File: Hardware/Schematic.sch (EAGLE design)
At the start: 89 parts, among them IC1 XC6220A331MR-G, IC2 BD5229G-TR, J1 SAMACSYS_PARTS_USB4110-GF-A, J2 FH34SRJ-24S-0.5SH_99_, J4 112A-TAAR-R03_ATTEND, Q1 20V/4.2A/52mΩ/1.4W, Q2 SI1308EDL-T1-GE3, Q3 20V/4.2A/52mΩ/1.4W, U1 ESP32_WROVER_SPARKFUN-IC-POWE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, U2 ESP32-C6-WROOM-1-N8, U3 ESP32_WROVER_BME680_BME680, U4 MAX17048G+T10, U5 DS3231SN#

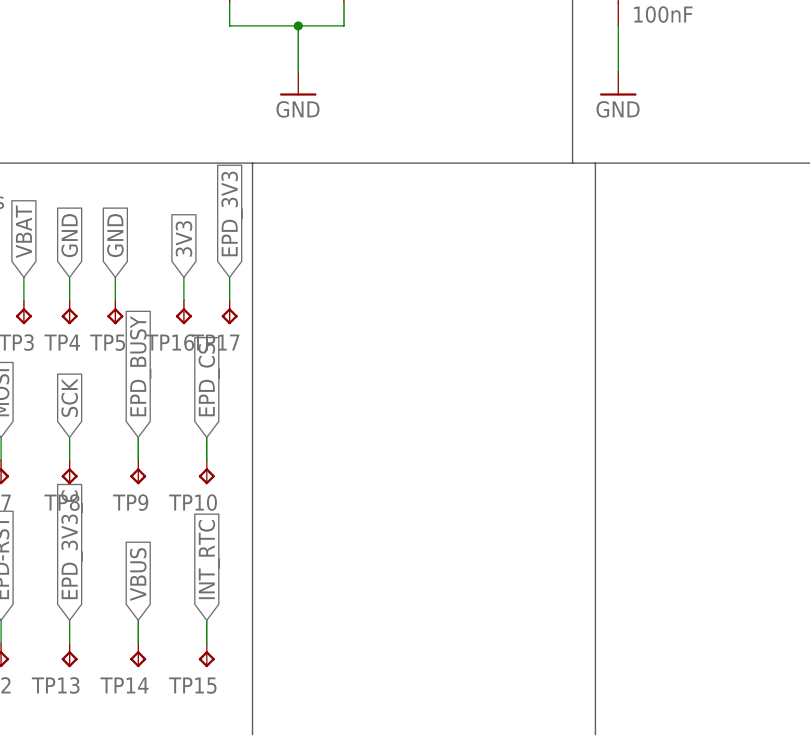
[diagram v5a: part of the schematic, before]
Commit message: add Qwiic /Stemma QT
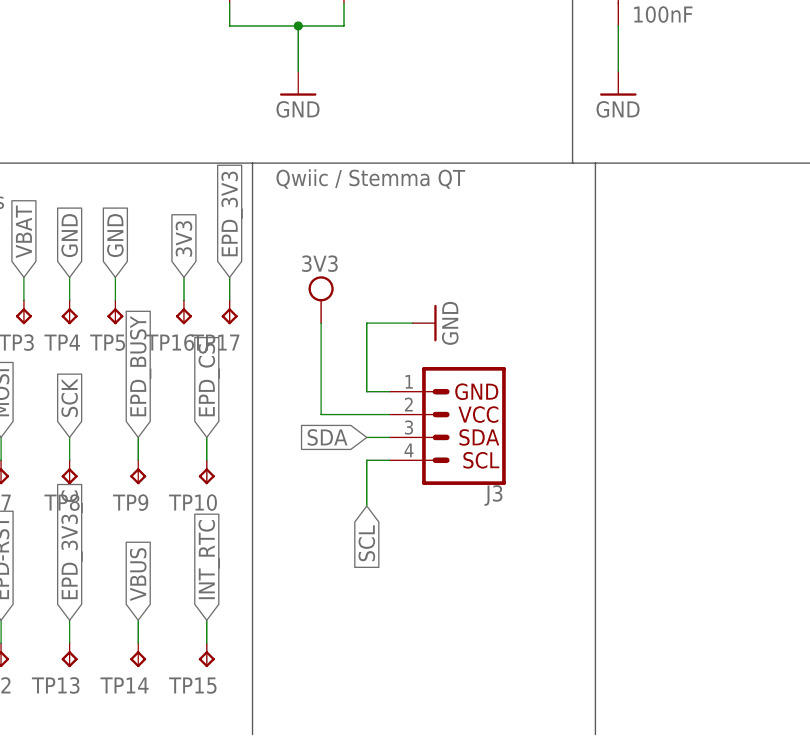
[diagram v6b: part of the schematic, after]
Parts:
- added J3: QWIIC_RIGHT_ANGLE, DeskAssistant v19 v1.flbr:QWIIC_CONNECTORJS-1MM
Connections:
- net 3V3: now also J3.2
- net GND: now also J3.1
- net SCL: now also J3.4
- net SDA: now also J3.3
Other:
- note added: "Qwiic / Stemma QT"
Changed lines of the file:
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@@
 <part name="TP16" library="DeskAssistant v19 v1.flbr" library_urn="urn:adsk.wipprod:fs.file:vf.vVvdDOfaSfavM5thX5SjWw" deviceset="TP" device="TP20R"/>
 <part name="TP17" library="DeskAssistant v19 v1.flbr" library_urn="urn:adsk.wipprod:fs.file:vf.vVvdDOfaSfavM5thX5SjWw" deviceset="TP" device="TP20R"/>
+<part name="J3" library="DeskAssistant v19 v1.flbr" library_urn="urn:adsk.wipprod:fs.file:vf.vVvdDOfaSfavM5thX5SjWw" deviceset="QWIIC_CONNECTOR" device="JS-1MM" package3d_urn="urn:adsk.eagle:package:41390393/1" value="QWIIC_RIGHT_ANGLE"/>
+<part name="SUPPLY14" library="DeskAssistant v19 v1.flbr" library_urn="urn:adsk.wipprod:fs.file:vf.vVvdDOfaSfavM5thX5SjWw" deviceset="3V3-CIRCLE" device="" value="3V3"/>
+<part name="GND41" library="DeskAssistant v19 v1.flbr" library_urn="urn:adsk.wipprod:fs.file:vf.vVvdDOfaSfavM5thX5SjWw" deviceset="GND" device=""/>
 </parts>
 <sheets>
@@
 <text x="-160.02" y="81.28" size="1.778" layer="95"> RTC Module DS3231SN</text>
 <text x="-10.16" y="81.28" size="1.778" layer="95">Test Pads</text>
+<text x="30.48" y="83.82" size="1.778" layer="95">Qwiic / Stemma QT</text>
 </plain>
 <instances>
@@
 <attribute name="NAME" x="26.67" y="67.31" size="1.778" layer="95" rot="R180"/>
 <attribute name="TP_SIGNAL_NAME" x="24.13" y="69.85" size="1.778" layer="97" rot="R180"/>
+</instance>
+<instance part="J3" gate="J1" x="50.8" y="58.42" smashed="yes" rot="R180">
+<attribute name="NAME" x="55.88" y="50.546" size="1.778" layer="95" font="vector" rot="R180"/>
+</instance>
+<instance part="SUPPLY14" gate="G$1" x="35.56" y="71.12" smashed="yes">
+<attribute name="VALUE" x="35.433" y="74.295" size="1.778" layer="96" align="bottom-center"/>
+</instance>
+<instance part="GND41" gate="1" x="48.26" y="68.58" smashed="yes" rot="R90">
+<attribute name="VALUE" x="50.8" y="66.04" size="1.778" layer="96" rot="R90"/>
 </instance>
 </instances>
@@
 <label x="12.7" y="73.66" size="1.778" layer="95" rot="R90" xref="yes"/>
 </segment>
+<segment>
+<pinref part="J3" gate="J1" pin="1"/>
+<wire x1="43.18" y1="60.96" x2="40.64" y2="60.96" width="0.1524" layer="91"/>
+<wire x1="40.64" y1="60.96" x2="40.64" y2="68.58" width="0.1524" layer="91"/>
+<wire x1="40.64" y1="68.58" x2="45.72" y2="68.58" width="0.1524" layer="91"/>
+<pinref part="GND41" gate="1" pin="GND"/>
+</segment>
 </net>
 <net name="VUSB" class="0">
@@
 <wire x1="20.32" y1="71.12" x2="20.32" y2="73.66" width="0.1524" layer="91"/>
 <label x="20.32" y="73.66" size="1.778" layer="95" rot="R90" xref="yes"/>
+</segment>
+<segment>
+<pinref part="J3" gate="J1" pin="2"/>
+<wire x1="43.18" y1="58.42" x2="35.56" y2="58.42" width="0.1524" layer="91"/>
+<wire x1="35.56" y1="58.42" x2="35.56" y2="68.58" width="0.1524" layer="91"/>
+<pinref part="SUPPLY14" gate="G$1" pin="3V3"/>
 </segment>
 </net>
@@
 <label x="-144.78" y="55.88" size="1.778" layer="95" rot="R180" xref="yes"/>
 </segment>
+<segment>
+<pinref part="J3" gate="J1" pin="3"/>
+<wire x1="43.18" y1="55.88" x2="40.64" y2="55.88" width="0.1524" layer="91"/>
+<label x="40.64" y="55.88" size="1.778" layer="95" rot="R180" xref="yes"/>
+</segment>
 </net>
 <net name="SCL" class="0">
@@
 <label x="-144.78" y="58.42" size="1.778" layer="95" rot="R180" xref="yes"/>
 </segment>
-</net>
+<segment>
+<pinref part="J3" gate="J1" pin="4"/>
+<wire x1="43.18" y1="53.34" x2="40.64" y2="53.34" width="0.1524" layer="91"/>
+<wire x1="40.64" y1="53.34" x2="40.64" y2="48.26" width="0.1524" layer="91"/>
+<label x="40.64" y="48.26" size="1.778" layer="95" rot="R270" xref="yes"/>
+</segment>
+</net>

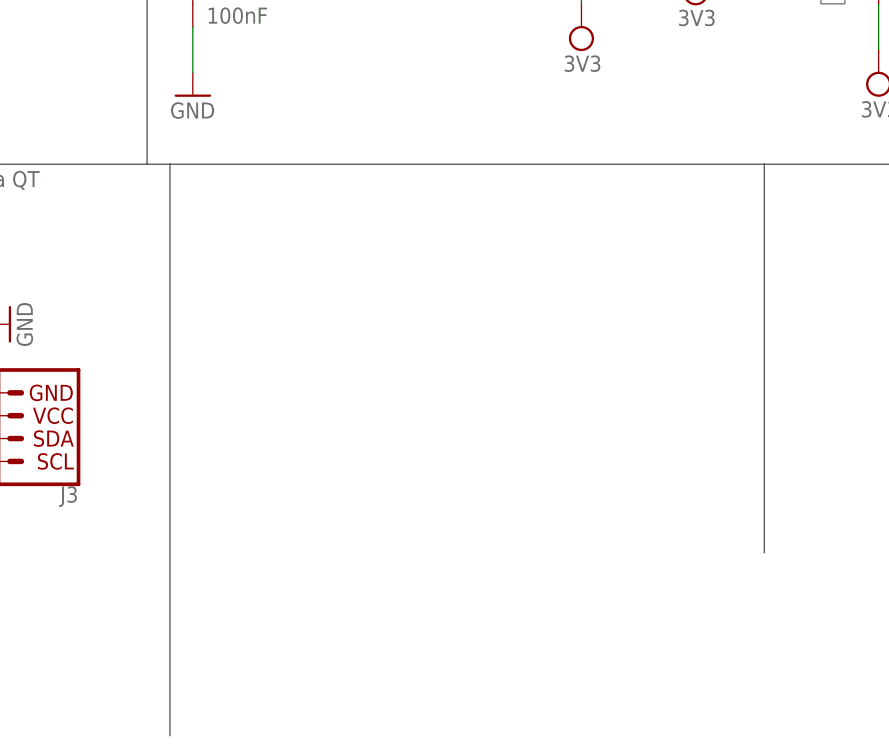
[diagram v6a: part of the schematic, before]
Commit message: add SPI ESD Protection Lines
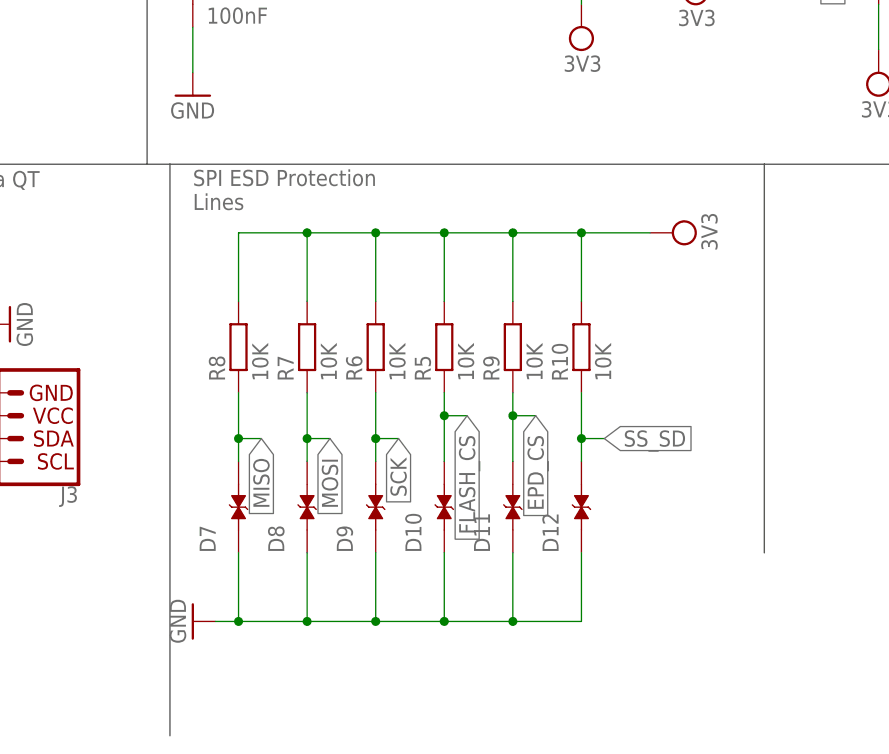
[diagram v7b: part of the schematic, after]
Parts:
- added D10, D11, D12, D7, D8, D9: PGB1010603MR, DeskAssistant v19 v1.flbr:PGB1010603MR
- added R10, R5, R6, R7, R8, R9: 10K, DeskAssistant v19 v1.flbr:ESP32_WROVER_EAGLE-LTSPICE_RR0402
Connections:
- net 3V3: now also R10.2, R5.2, R6.2, R7.2, R8.2, R9.2
- net EPD_CS: now also D11.2, R9.1
- net FLASH_CS: now also D10.2, R5.1
- net GND: now also D10.1, D11.1, D12.1, D7.1, D8.1, D9.1
- net MISO: now also D7.2, R8.1
- net MOSI: now also D8.2, R7.1
- net SCK: now also D9.2, R6.1
- net SS_SD: now also D12.2, R10.1
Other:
- note added: "SPI ESD Protection Lines"

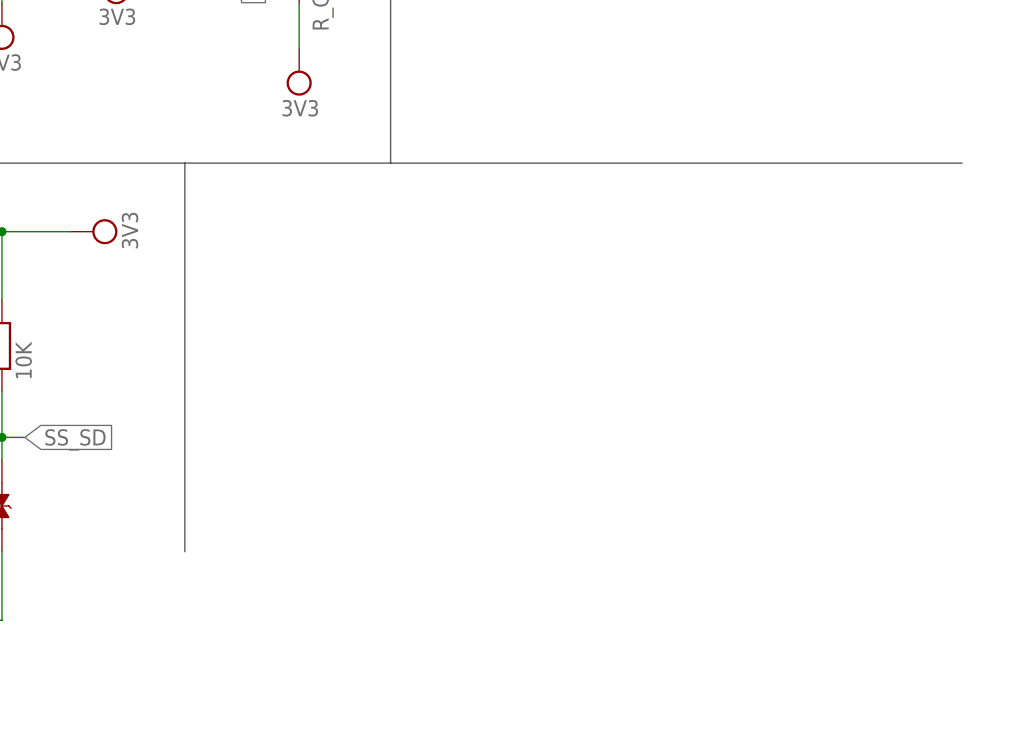
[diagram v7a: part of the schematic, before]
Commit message: add External NOR Flash 64MB and finish schematic
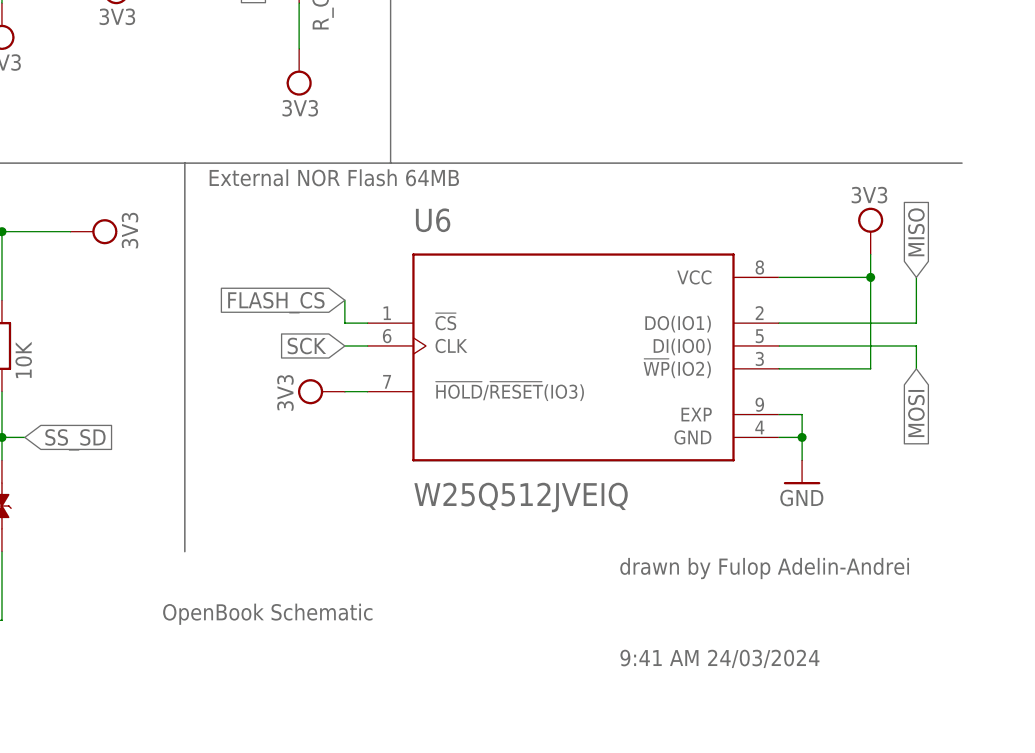
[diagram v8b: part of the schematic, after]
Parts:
- added U6: W25Q512JVEIQ, DeskAssistant v19 v1.flbr:W25Q512JVEIQ
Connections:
- net 3V3: now also U6.!HOLD!/!RESET!(IO3), U6.!WP!(IO2), U6.VCC
- net FLASH_CS: now also U6.!CS
- net GND: now also U6.EXP, U6.GND
- net MISO: now also U6.DO(IO1)
- net MOSI: now also U6.DI(IO0)
- net SCK: now also U6.CLK
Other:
- note added: "9:41 AM 24/03/2024"
- note added: "External NOR Flash 64MB"
- note added: "OpenBook Schematic"
- note added: "drawn by Fulop Adelin-Andrei"
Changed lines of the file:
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@@
 <part name="D11" library="DeskAssistant v19 v1.flbr" library_urn="urn:adsk.wipprod:fs.file:vf.vVvdDOfaSfavM5thX5SjWw" deviceset="PGB1010603MR" device=""/>
 <part name="D12" library="DeskAssistant v19 v1.flbr" library_urn="urn:adsk.wipprod:fs.file:vf.vVvdDOfaSfavM5thX5SjWw" deviceset="PGB1010603MR" device=""/>
+<part name="U6" library="DeskAssistant v19 v1.flbr" library_urn="urn:adsk.wipprod:fs.file:vf.vVvdDOfaSfavM5thX5SjWw" deviceset="W25Q512JVEIQ" device=""/>
+<part name="SUPPLY16" library="DeskAssistant v19 v1.flbr" library_urn="urn:adsk.wipprod:fs.file:vf.vVvdDOfaSfavM5thX5SjWw" deviceset="3V3-CIRCLE" device="" value="3V3"/>
+<part name="GND43" library="DeskAssistant v19 v1.flbr" library_urn="urn:adsk.wipprod:fs.file:vf.vVvdDOfaSfavM5thX5SjWw" deviceset="GND" device=""/>
+<part name="SUPPLY17" library="DeskAssistant v19 v1.flbr" library_urn="urn:adsk.wipprod:fs.file:vf.vVvdDOfaSfavM5thX5SjWw" deviceset="3V3-CIRCLE" device="" value="3V3"/>
 </parts>
 <sheets>
@@
 <text x="68.58" y="81.28" size="1.778" layer="95">SPI ESD Protection
 Lines</text>
+<text x="134.62" y="83.82" size="1.778" layer="95">External NOR Flash 64MB</text>
+<text x="129.54" y="35.56" size="1.778" layer="95">OpenBook Schematic</text>
+<text x="180.34" y="40.64" size="1.778" layer="95">drawn by Fulop Adelin-Andrei</text>
+<text x="180.34" y="30.48" size="1.778" layer="95">9:41 AM 24/03/2024</text>
 </plain>
 <instances>
 <instance part="FRAME1" gate="G$1" x="-165.1" y="20.32" smashed="yes">
 <attribute name="DRAWING_NAME" x="179.07" y="35.56" size="2.54" layer="94"/>
-<attribute name="LAST_DATE_TIME" x="179.07" y="30.48" size="2.286" layer="94"/>
 <attribute name="SHEET" x="192.405" y="25.4" size="2.54" layer="94"/>
 </instance>
@@
 <instance part="D12" gate="G$1" x="111.76" y="48.26" smashed="yes" rot="R90">
 <attribute name="NAME" x="109.22" y="43.18" size="1.778" layer="95" rot="R90"/>
+</instance>
+<instance part="U6" gate="G$1" x="175.26" y="63.5" smashed="yes">
+<attribute name="NAME" x="157.48" y="78.74" size="2.54" layer="95"/>
+<attribute name="VALUE" x="157.48" y="48.26" size="2.54" layer="96"/>
+</instance>
+<instance part="SUPPLY16" gate="G$1" x="147.32" y="60.96" smashed="yes" rot="R90">
+<attribute name="VALUE" x="144.145" y="60.833" size="1.778" layer="96" rot="R90" align="bottom-center"/>
+</instance>
+<instance part="GND43" gate="1" x="200.66" y="50.8" smashed="yes">
+<attribute name="VALUE" x="198.12" y="48.26" size="1.778" layer="96"/>
+</instance>
+<instance part="SUPPLY17" gate="G$1" x="208.28" y="78.74" smashed="yes">
+<attribute name="VALUE" x="208.153" y="81.915" size="1.778" layer="96" align="bottom-center"/>
 </instance>
 </instances>
@@
 <junction x="81.28" y="35.56"/>
 </segment>
+<segment>
+<pinref part="U6" gate="G$1" pin="EXP"/>
+<wire x1="198.12" y1="58.42" x2="200.66" y2="58.42" width="0.1524" layer="91"/>
+<wire x1="200.66" y1="58.42" x2="200.66" y2="55.88" width="0.1524" layer="91"/>
+<wire x1="200.66" y1="55.88" x2="198.12" y2="55.88" width="0.1524" layer="91"/>
+<pinref part="U6" gate="G$1" pin="GND"/>
+<wire x1="200.66" y1="55.88" x2="200.66" y2="53.34" width="0.1524" layer="91"/>
+<junction x="200.66" y="55.88"/>
+<pinref part="GND43" gate="1" pin="GND"/>
+</segment>
 </net>
 <net name="VUSB" class="0">
@@
 <junction x="111.76" y="78.74"/>
 </segment>
+<segment>
+<pinref part="U6" gate="G$1" pin="!HOLD!/!RESET!(IO3)"/>
+<wire x1="152.4" y1="60.96" x2="149.86" y2="60.96" width="0.1524" layer="91"/>
+<pinref part="SUPPLY16" gate="G$1" pin="3V3"/>
+</segment>
+<segment>
+<pinref part="U6" gate="G$1" pin="!WP!(IO2)"/>
+<wire x1="198.12" y1="63.5" x2="208.28" y2="63.5" width="0.1524" layer="91"/>
+<wire x1="208.28" y1="63.5" x2="208.28" y2="73.66" width="0.1524" layer="91"/>
+<wire x1="208.28" y1="73.66" x2="198.12" y2="73.66" width="0.1524" layer="91"/>
+<pinref part="U6" gate="G$1" pin="VCC"/>
+<wire x1="208.28" y1="73.66" x2="208.28" y2="76.2" width="0.1524" layer="91"/>
+<junction x="208.28" y="73.66"/>
+<pinref part="SUPPLY17" gate="G$1" pin="3V3"/>
+</segment>
 </net>
 <net name="N$3" class="0">
@@
 <label x="83.82" y="55.88" size="1.778" layer="95" rot="R270" xref="yes"/>
 </segment>
+<segment>
+<pinref part="U6" gate="G$1" pin="DI(IO0)"/>
+<wire x1="198.12" y1="66.04" x2="213.36" y2="66.04" width="0.1524" layer="91"/>
+<wire x1="213.36" y1="66.04" x2="213.36" y2="63.5" width="0.1524" layer="91"/>
+<label x="213.36" y="63.5" size="1.778" layer="95" rot="R270" xref="yes"/>
+</segment>
 </net>
 <net name="MISO" class="0">
@@
 <label x="76.2" y="55.88" size="1.778" layer="95" rot="R270" xref="yes"/>
 </segment>
+<segment>
+<pinref part="U6" gate="G$1" pin="DO(IO1)"/>
+<wire x1="198.12" y1="68.58" x2="213.36" y2="68.58" width="0.1524" layer="91"/>
+<wire x1="213.36" y1="68.58" x2="213.36" y2="73.66" width="0.1524" layer="91"/>
+<label x="213.36" y="73.66" size="1.778" layer="95" rot="R90" xref="yes"/>
+</segment>
 </net>
 <net name="SCK" class="0">
@@
 <wire x1="88.9" y1="55.88" x2="91.44" y2="55.88" width="0.1524" layer="91"/>
 <label x="91.44" y="55.88" size="1.778" layer="95" rot="R270" xref="yes"/>
+</segment>
+<segment>
+<pinref part="U6" gate="G$1" pin="CLK"/>
+<wire x1="152.4" y1="66.04" x2="149.86" y2="66.04" width="0.1524" layer="91"/>
+<label x="149.86" y="66.04" size="1.778" layer="95" rot="R180" xref="yes"/>
 </segment>
 </net>
@@
 <label x="99.06" y="58.42" size="1.778" layer="95" rot="R270" xref="yes"/>
 </segment>
-</net>
+<segment>
+<pinref part="U6" gate="G$1" pin="!CS"/>
+<wire x1="152.4" y1="68.58" x2="149.86" y2="68.58" width="0.1524" layer="91"/>
+<wire x1="149.86" y1="68.58" x2="149.86" y2="71.12" width="0.1524" layer="91"/>
+<label x="149.86" y="71.12" size="1.778" layer="95" rot="R180" xref="yes"/>
+</segment>
+</net>
